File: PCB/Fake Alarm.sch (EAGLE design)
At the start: 12 parts, among them IC1 NE555DG4

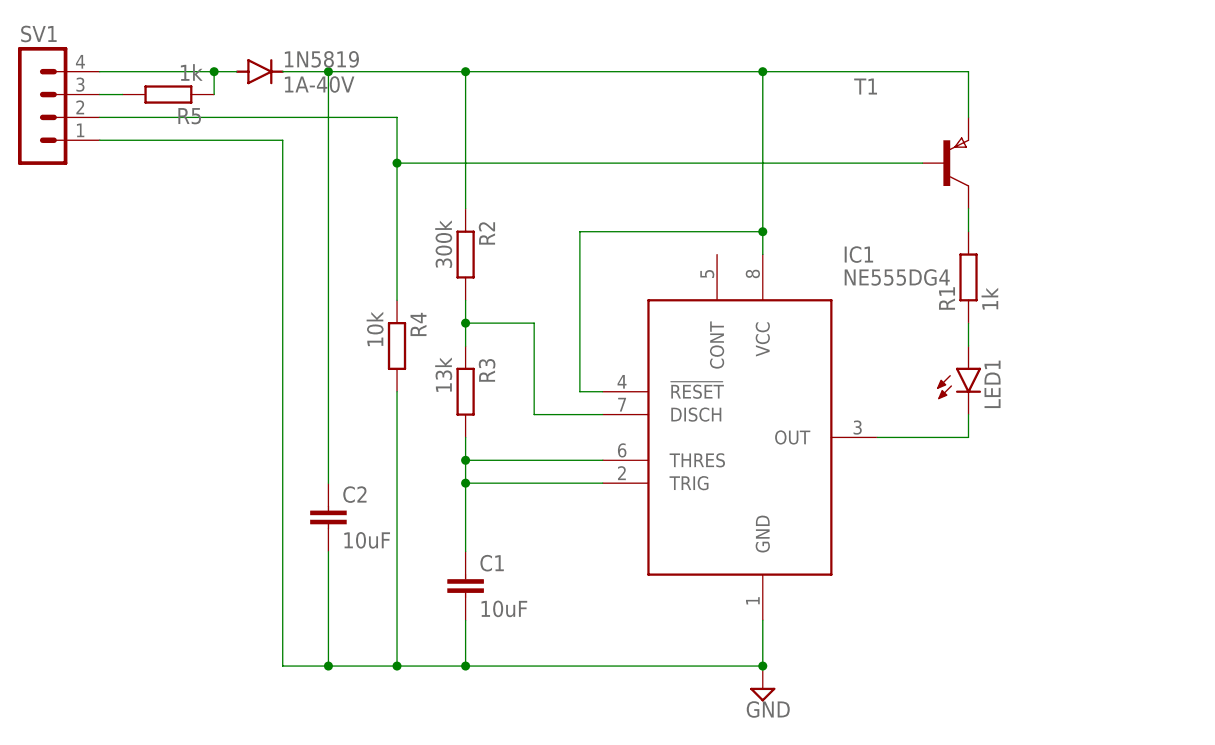
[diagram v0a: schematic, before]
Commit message: New Design Fake Alarm Schematic and Layout
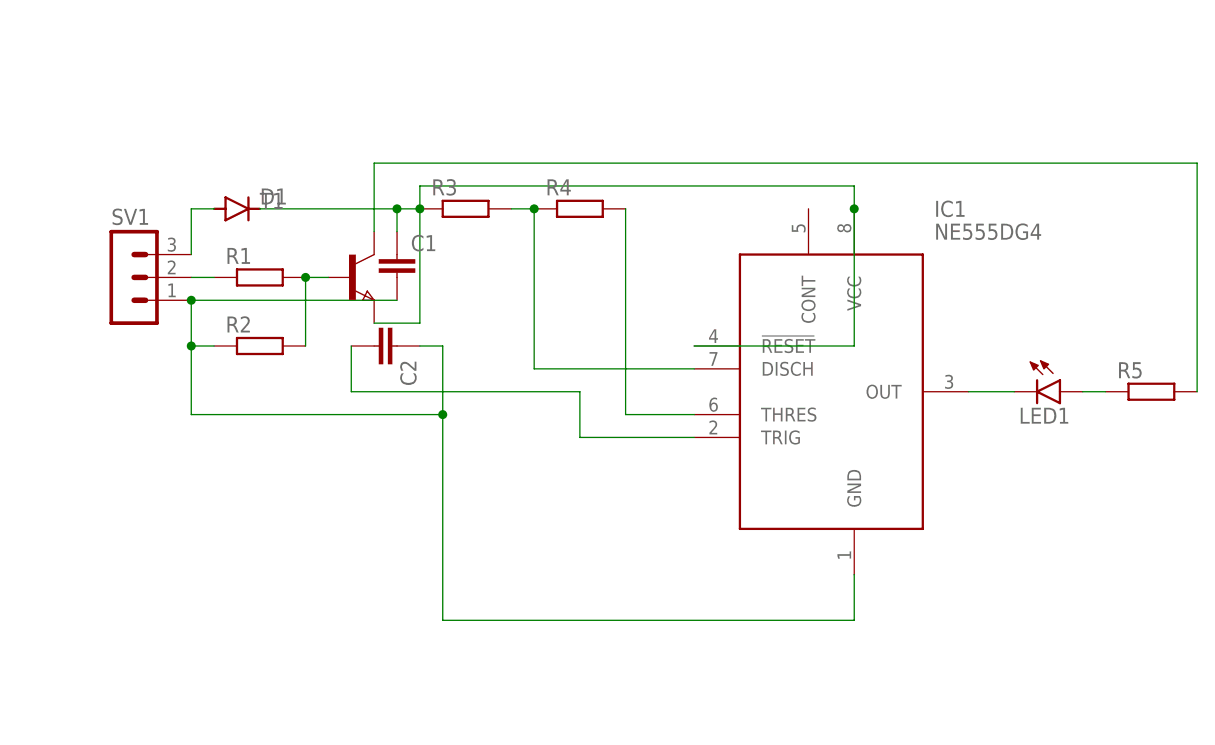
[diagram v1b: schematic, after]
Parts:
- removed 1N5819: 1A-40V, diode:DIODE-DO214AC
- added D1: (no value), diode:DIODE-DO-214AC
- C1, C2: value 10uF -> (none); device rcl:C-EUC0805K -> rcl:C-EUC0805
- LED1: device led:LEDCHIP-LED0805 -> led:LEDKA-3528ASYC
- R1, R5: value 1k -> (none)
- R2: value 300k -> (none)
- R3: value 13k -> (none)
- R4: value 10k -> (none)
- SV1: device con-lstb:MA04-1 -> con-lstb:MA03-1
- T1: device zetex:PNPSOT23 -> zetex:NPNSOT23
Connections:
- removed net GND: C1.2, C2.2, IC1.GND, R4.2, SV1.1
- removed net N$8 (its old number): R5.2, SV1.3
- new net N$10: R5.2, T1.C
- new net N$11: IC1.THRES, R4.2
- new net N$2: R1.1, SV1.2
- net N$1: now also D1.A, SV1.3; no longer 1N5819.C, C2.1, IC1.!RESET, IC1.VCC, R2.1, T1.E
- net N$3: now also C1.2, C2.1, IC1.GND, R2.1, SV1.1; no longer LED1.A, R1.1
- net N$4: now also C1.1, D1.C, IC1.!RESET, IC1.VCC, R3.1, T1.E; no longer R1.2, T1.C
- net N$5: now also R1.2, R2.2; no longer R4.1, SV1.2
- net N$6: now also R3.2, R4.1; no longer R2.2, R3.1
- net N$7: now also C2.2; no longer C1.1, IC1.THRES, R3.2
- net N$9: now also LED1.A; no longer 1N5819.A, SV1.4
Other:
- moved on the sheet: C1, C2, IC1, LED1, R1, R2, R3, R4, R5, T1
